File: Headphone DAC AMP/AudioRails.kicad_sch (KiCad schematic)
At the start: 39 parts, among them U11 ADP5071AREZ-R7, U12 TPS74501PDRVR, U14 ADP7185ACPZN-R7

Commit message: Swapped to 0603 caps in order to compact design
Planning on a 100x70mm board shape
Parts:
- C33, C34, C35, C36, C37, C38, C40, C41, C42, C43, C50, C51, C52, C53, C54, C55: footprint Capacitor_SMD:C_0805_2012Metric_Pad1.18x1.45mm_HandSolder -> Capacitor_SMD:C_0603_1608Metric_Pad1.08x0.95mm_HandSolder
- D1, D2: footprint Diode_SMD:D_0805_2012Metric_Pad1.15x1.40mm_HandSolder -> Capacitor_SMD:C_0603_1608Metric_Pad1.08x0.95mm_HandSolder
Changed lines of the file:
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@@
 			)
 		)
-		(property "Footprint" "Capacitor_SMD:C_0805_2012Metric_Pad1.18x1.45mm_HandSolder"
+		(property "Footprint" "Capacitor_SMD:C_0603_1608Metric_Pad1.08x0.95mm_HandSolder"
 			(at 50.4952 68.58 0)
 			(effects
@@
 			)
 		)
-		(property "Footprint" "Capacitor_SMD:C_0805_2012Metric_Pad1.18x1.45mm_HandSolder"
+		(property "Footprint" "Capacitor_SMD:C_0603_1608Metric_Pad1.08x0.95mm_HandSolder"
 			(at 28.9052 130.81 0)
 			(effects
@@
 			)
 		)
-		(property "Footprint" "Capacitor_SMD:C_0805_2012Metric_Pad1.18x1.45mm_HandSolder"
+		(property "Footprint" "Capacitor_SMD:C_0603_1608Metric_Pad1.08x0.95mm_HandSolder"
 			(at 185.1152 134.62 0)
 			(effects
@@
 			)
 		)
-		(property "Footprint" "Capacitor_SMD:C_0805_2012Metric_Pad1.18x1.45mm_HandSolder"
+		(property "Footprint" "Capacitor_SMD:C_0603_1608Metric_Pad1.08x0.95mm_HandSolder"
 			(at 55.5752 33.02 0)
 			(effects
@@
 			)
 		)
-		(property "Footprint" "Capacitor_SMD:C_0805_2012Metric_Pad1.18x1.45mm_HandSolder"
+		(property "Footprint" "Capacitor_SMD:C_0603_1608Metric_Pad1.08x0.95mm_HandSolder"
 			(at 142.24 42.2148 0)
 			(effects
@@
 			)
 		)
-		(property "Footprint" "Capacitor_SMD:C_0805_2012Metric_Pad1.18x1.45mm_HandSolder"
+		(property "Footprint" "Capacitor_SMD:C_0603_1608Metric_Pad1.08x0.95mm_HandSolder"
 			(at 130.5052 73.66 0)
 			(effects
@@
 			)
 		)
-		(property "Footprint" "Capacitor_SMD:C_0805_2012Metric_Pad1.18x1.45mm_HandSolder"
+		(property "Footprint" "Capacitor_SMD:C_0603_1608Metric_Pad1.08x0.95mm_HandSolder"
 			(at 247.3452 132.08 0)
 			(effects
@@
 			)
 		)
-		(property "Footprint" "Capacitor_SMD:C_0805_2012Metric_Pad1.18x1.45mm_HandSolder"
+		(property "Footprint" "Capacitor_SMD:C_0603_1608Metric_Pad1.08x0.95mm_HandSolder"
 			(at 174.9552 134.62 0)
 			(effects
@@
 			)
 		)
-		(property "Footprint" "Capacitor_SMD:C_0805_2012Metric_Pad1.18x1.45mm_HandSolder"
+		(property "Footprint" "Capacitor_SMD:C_0603_1608Metric_Pad1.08x0.95mm_HandSolder"
 			(at 159.7152 45.72 0)
 			(effects
@@
 			)
 		)
-		(property "Footprint" "Capacitor_SMD:C_0805_2012Metric_Pad1.18x1.45mm_HandSolder"
+		(property "Footprint" "Capacitor_SMD:C_0603_1608Metric_Pad1.08x0.95mm_HandSolder"
 			(at 40.3352 130.81 0)
 			(effects
@@
 			)
 		)
-		(property "Footprint" "Capacitor_SMD:C_0805_2012Metric_Pad1.18x1.45mm_HandSolder"
+		(property "Footprint" "Capacitor_SMD:C_0603_1608Metric_Pad1.08x0.95mm_HandSolder"
 			(at 63.1952 140.97 0)
 			(effects
@@
 			)
 		)
-		(property "Footprint" "Capacitor_SMD:C_0805_2012Metric_Pad1.18x1.45mm_HandSolder"
+		(property "Footprint" "Capacitor_SMD:C_0603_1608Metric_Pad1.08x0.95mm_HandSolder"
 			(at 125.4252 33.02 0)
 			(effects
@@
 			)
 		)
-		(property "Footprint" "Capacitor_SMD:C_0805_2012Metric_Pad1.18x1.45mm_HandSolder"
+		(property "Footprint" "Capacitor_SMD:C_0603_1608Metric_Pad1.08x0.95mm_HandSolder"
 			(at 130.5052 132.08 0)
 			(effects
@@
 			)
 		)
-		(property "Footprint" "Capacitor_SMD:C_0805_2012Metric_Pad1.18x1.45mm_HandSolder"
+		(property "Footprint" "Capacitor_SMD:C_0603_1608Metric_Pad1.08x0.95mm_HandSolder"
 			(at 120.3452 132.08 0)
 			(effects
@@
 			)
 		)
-		(property "Footprint" "Diode_SMD:D_0805_2012Metric_Pad1.15x1.40mm_HandSolder"
+		(property "Footprint" "Capacitor_SMD:C_0603_1608Metric_Pad1.08x0.95mm_HandSolder"
 			(at 43.18 33.02 0)
 			(effects
@@
 			)
 		)
-		(property "Footprint" "Capacitor_SMD:C_0805_2012Metric_Pad1.18x1.45mm_HandSolder"
+		(property "Footprint" "Capacitor_SMD:C_0603_1608Metric_Pad1.08x0.95mm_HandSolder"
 			(at 257.5052 132.08 0)
 			(effects
@@
 			)
 		)
-		(property "Footprint" "Capacitor_SMD:C_0805_2012Metric_Pad1.18x1.45mm_HandSolder"
+		(property "Footprint" "Capacitor_SMD:C_0603_1608Metric_Pad1.08x0.95mm_HandSolder"
 			(at 143.2052 132.08 0)
 			(effects
@@
 			)
 		)
-		(property "Footprint" "Diode_SMD:D_0805_2012Metric_Pad1.15x1.40mm_HandSolder"
+		(property "Footprint" "Capacitor_SMD:C_0603_1608Metric_Pad1.08x0.95mm_HandSolder"
 			(at 138.43 33.02 0)
 			(effects

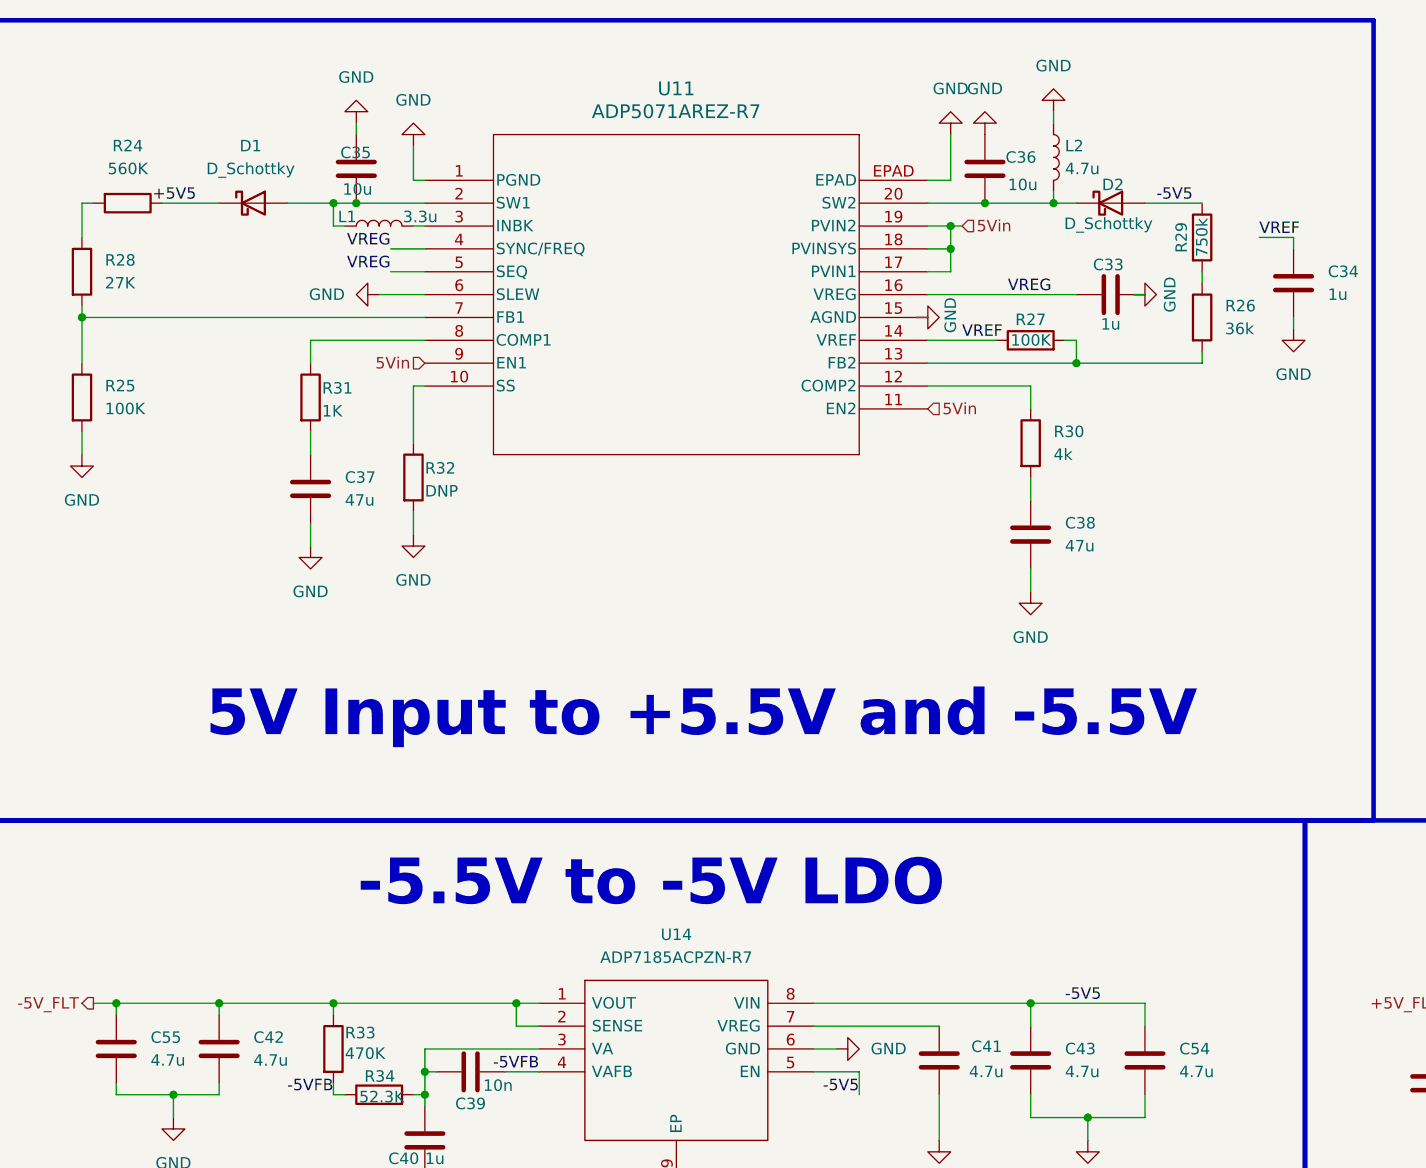
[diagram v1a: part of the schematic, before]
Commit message: Defined board shape and redid ADP5071 layout
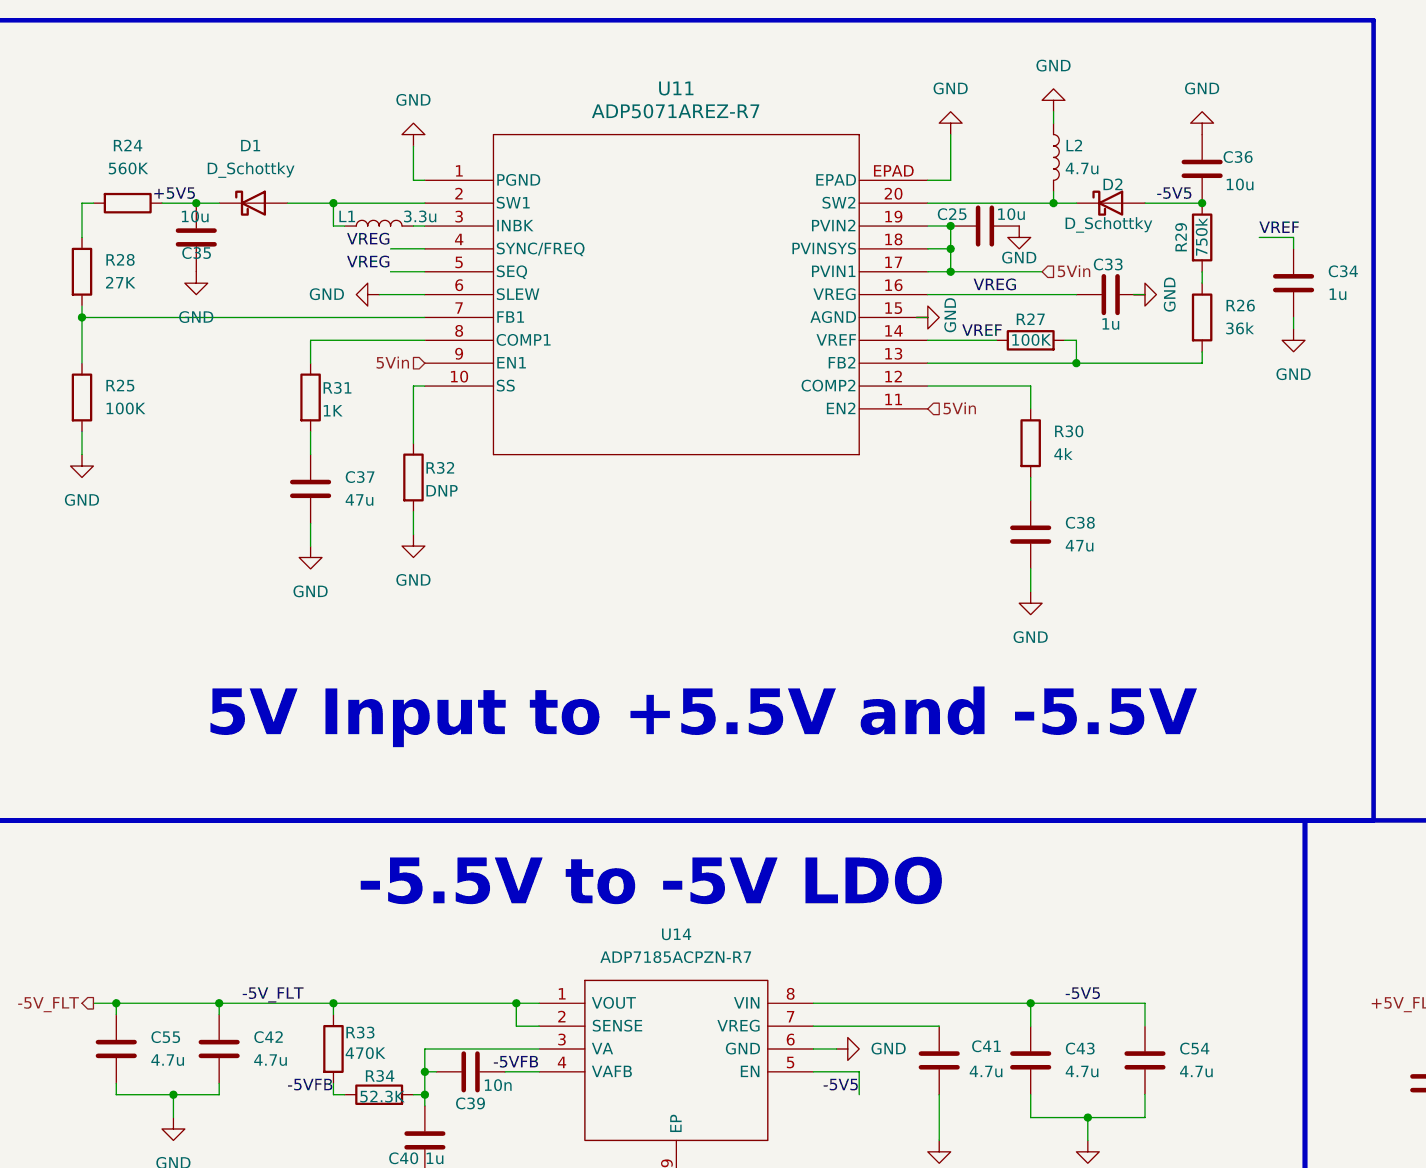
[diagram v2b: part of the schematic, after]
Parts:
- added C25: 10u, Capacitor_SMD:C_0603_1608Metric_Pad1.08x0.95mm_HandSolder, symbol Device:C
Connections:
- net +5V5: now also C35.2
- net -5V5: now also C36.2
- net 5Vin: now also C25.2
- net GND: now also C25.1
- net at D1.2 (A), L1.1, U11.2 (SW1): no longer C35.2
- net at D2.1 (K), L2.2, U11.20 (SW2): no longer C36.2
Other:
- moved on the sheet: C35, C36
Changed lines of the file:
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@@
 	)
 	(junction
+		(at 148.59 33.02)
+		(diameter 0)
+		(color 0 0 0 0)
+	)
+	(junction
 		(at 120.65 38.1)
 		(diameter 0)
@@
 	)
 	(junction
+		(at 120.65 40.64)
+		(diameter 0)
+		(color 0 0 0 0)
+	)
+	(junction
 		(at 62.23 132.08)
 		(diameter 0)
@@
 	)
 	(junction
-		(at 54.61 33.02)
-		(diameter 0)
-		(color 0 0 0 0)
-	)
-	(junction
 		(at 135.89 134.62)
 		(diameter 0)
@@
 	)
 	(junction
-		(at 124.46 33.02)
+		(at 36.83 33.02)
 		(diameter 0)
 		(color 0 0 0 0)
@@
 	(wire
 		(pts
-			(xy 54.61 24.13) (xy 54.61 25.4)
-		)
-		(stroke
-			(width 0)
-			(type default)
-		)
-	)
-	(wire
-		(pts
 			(xy 179.07 135.89) (xy 184.15 135.89)
 		)
@@
 	(wire
 		(pts
-			(xy 33.02 33.02) (xy 39.37 33.02)
+			(xy 33.02 33.02) (xy 36.83 33.02)
 		)
 		(stroke
@@
 	(wire
 		(pts
-			(xy 120.65 35.56) (xy 121.92 35.56)
+			(xy 120.65 40.64) (xy 130.81 40.64)
 		)
 		(stroke
@@
 	(wire
 		(pts
+			(xy 120.65 38.1) (xy 120.65 35.56)
+		)
+		(stroke
+			(width 0)
+			(type default)
+		)
+	)
+	(wire
+		(pts
 			(xy 270.51 135.89) (xy 270.51 137.16)
 		)
@@
 	(wire
 		(pts
-			(xy 124.46 33.02) (xy 132.08 33.02)
+			(xy 118.11 33.02) (xy 132.08 33.02)
 		)
 		(stroke
@@
 	(wire
 		(pts
-			(xy 52.07 33.02) (xy 54.61 33.02)
+			(xy 52.07 33.02) (xy 62.23 33.02)
 		)
 		(stroke
@@
 	(wire
 		(pts
-			(xy 118.11 33.02) (xy 124.46 33.02)
-		)
-		(stroke
-			(width 0)
-			(type default)
-		)
-	)
-	(wire
-		(pts
 			(xy 58.42 38.1) (xy 62.23 38.1)
 		)
@@
 	(wire
 		(pts
-			(xy 120.65 35.56) (xy 120.65 38.1)
-		)
-		(stroke
-			(width 0)
-			(type default)
-		)
-	)
-	(wire
-		(pts
-			(xy 54.61 33.02) (xy 62.23 33.02)
+			(xy 36.83 33.02) (xy 39.37 33.02)
 		)
 		(stroke
@@
 	)
 	(label "VREG"
-		(at 127 43.18 0)
+		(at 123.19 43.18 0)
 		(effects
 			(font
@@
 		)
 	)
+	(label "-5V_FLT"
+		(at 41.91 121.92 0)
+		(effects
+			(font
+				(size 1.27 1.27)
+			)
+			(justify left bottom)
+		)
+	)
 	(label "5VFB"
 		(at 198.12 124.46 0)
@@
 	(hierarchical_label "5Vin"
 		(shape input)
-		(at 121.92 35.56 0)
+		(at 130.81 40.64 0)
 		(effects
 			(font
@@
 	)
 	(symbol
+		(lib_id "Device:C")
+		(at 124.46 35.56 270)
+		(unit 1)
+		(exclude_from_sim no)
+		(in_bom yes)
+		(on_board yes)
+		(dnp no)
+		(property "Reference" "C25"
+			(at 119.126 34.29 90)
+			(effects
+				(font
+					(size 1.27 1.27)
+				)
+				(justify left)
+			)
+		)
+		(property "Value" "10u"
+			(at 125.73 34.29 90)
+			(effects
+				(font
+					(size 1.27 1.27)
+				)
+				(justify left)
+			)
+		)
+		(property "Footprint" "Capacitor_SMD:C_0603_1608Metric_Pad1.08x0.95mm_HandSolder"
+			(at 120.65 36.5252 0)
+			(effects
+				(font
+					(size 1.27 1.27)
+				)
+				(hide yes)
+			)
+		)
+		(property "Datasheet" "~"
+			(at 124.46 35.56 0)
+			(effects
+				(font
+					(size 1.27 1.27)
+				)
+				(hide yes)
+			)
+		)
+		(property "Description" "Unpolarized capacitor"
+			(at 124.46 35.56 0)
+			(effects
+				(font
+					(size 1.27 1.27)
+				)
+				(hide yes)
+			)
+		)
+		(pin "2"
+		)
+		(pin "1"
+		)
+		(instances
+			(project "Headphone DAC AMP"
+				(path "/d034eddd-efbc-47be-a25c-37cbfbab4cd8/22bf93f4-b6c7-483e-b255-2ccf5bc3f52b"
+					(reference "C25")
+					(unit 1)
+				)
+			)
+		)
+	)
+	(symbol
 		(lib_id "power:GND")
 		(at 270.51 137.16 0)
@@
 	(symbol
 		(lib_id "Device:C")
-		(at 54.61 29.21 0)
+		(at 36.83 36.83 180)
 		(unit 1)
 		(exclude_from_sim no)
@@
 		(dnp no)
 		(property "Reference" "C35"
-			(at 52.832 27.432 0)
+			(at 38.608 38.608 0)
 			(effects
 				(font
@@
 		)
 		(property "Value" "10u"
-			(at 53.086 31.496 0)
+			(at 38.354 34.544 0)
 			(effects
 				(font
@@
 		)
 		(property "Footprint" "Capacitor_SMD:C_0603_1608Metric_Pad1.08x0.95mm_HandSolder"
-			(at 55.5752 33.02 0)
+			(at 35.8648 33.02 0)
 			(effects
 				(font
@@
 		)
 		(property "Datasheet" "~"
-			(at 54.61 29.21 0)
+			(at 36.83 36.83 0)
 			(effects
 				(font
@@
 		)
 		(property "Description" "Unpolarized capacitor"
-			(at 54.61 29.21 0)
+			(at 36.83 36.83 0)
 			(effects
 				(font
@@
 	(symbol
 		(lib_id "power:GND")
-		(at 124.46 25.4 180)
+		(at 148.59 25.4 180)
 		(unit 1)
 		(exclude_from_sim no)
@@
 		(fields_autoplaced yes)
 		(property "Reference" "#PWR043"
-			(at 124.46 19.05 0)
+			(at 148.59 19.05 0)
 			(effects
 				(font
@@
 		)
 		(property "Value" "GND"
-			(at 124.46 20.32 0)
+			(at 148.59 20.32 0)
 			(effects
 				(font
@@
 		)
 		(property "Footprint" ""
-			(at 124.46 25.4 0)
+			(at 148.59 25.4 0)
 			(effects
 				(font
@@
 		)
 		(property "Datasheet" ""
-			(at 124.46 25.4 0)
+			(at 148.59 25.4 0)
 			(effects
 				(font
@@
 		)
 		(property "Description" "Power symbol creates a global label with name \"GND\" , ground"
-			(at 124.46 25.4 0)
+			(at 148.59 25.4 0)
 			(effects
 				(font
@@
 	(symbol
 		(lib_id "Device:C")
-		(at 124.46 29.21 0)
+		(at 148.59 29.21 0)
 		(unit 1)
 		(exclude_from_sim no)
@@
 		(dnp no)
 		(property "Reference" "C36"
-			(at 126.746 27.94 0)
+			(at 150.876 27.94 0)
 			(effects
 				(font
@@
 		)
 		(property "Value" "10u"
-			(at 127 30.988 0)
+			(at 151.13 30.988 0)
 			(effects
 				(font
@@
 		)
 		(property "Footprint" "Capacitor_SMD:C_0603_1608Metric_Pad1.08x0.95mm_HandSolder"
-			(at 125.4252 33.02 0)
+			(at 149.5552 33.02 0)
 			(effects
 				(font
@@
 		)
 		(property "Datasheet" "~"
-			(at 124.46 29.21 0)
+			(at 148.59 29.21 0)
 			(effects
 				(font
@@
 		)
 		(property "Description" "Unpolarized capacitor"
-			(at 124.46 29.21 0)
+			(at 148.59 29.21 0)
 			(effects
 				(font
@@
 	(symbol
 		(lib_id "power:GND")
-		(at 54.61 24.13 180)
+		(at 36.83 40.64 0)
 		(unit 1)
 		(exclude_from_sim no)
@@
 		(fields_autoplaced yes)
 		(property "Reference" "#PWR042"
-			(at 54.61 17.78 0)
+			(at 36.83 46.99 0)
 			(effects
 				(font
@@
 		)
 		(property "Value" "GND"
-			(at 54.61 19.05 0)
+			(at 36.83 45.72 0)
 			(effects
 				(font
@@
 		)
 		(property "Footprint" ""
-			(at 54.61 24.13 0)
+			(at 36.83 40.64 0)
 			(effects
 				(font
@@
 		)
 		(property "Datasheet" ""
-			(at 54.61 24.13 0)
+			(at 36.83 40.64 0)
 			(effects
 				(font
@@
 		)
 		(property "Description" "Power symbol creates a global label with name \"GND\" , ground"
-			(at 54.61 24.13 0)
+			(at 36.83 40.64 0)
 			(effects
 				(font
@@
 					(unit 1)
 				)
+			)
+		)
+	)
+	(symbol
+		(lib_id "power:GND")
+		(at 128.27 35.56 0)
+		(unit 1)
+		(exclude_from_sim no)
+		(in_bom yes)
+		(on_board yes)
+		(dnp no)
+		(property "Reference" "#PWR031"
+			(at 128.27 41.91 0)
+			(effects
+				(font
+					(size 1.27 1.27)
+				)
+				(hide yes)
+			)
+		)
+		(property "Value" "GND"
+			(at 128.27 39.116 0)
+			(effects
+				(font
+					(size 1.27 1.27)
+				)
+			)
+		)
+		(property "Footprint" ""
+			(at 128.27 35.56 0)
+			(effects
+				(font
+					(size 1.27 1.27)
+				)
+				(hide yes)
+			)
+		)
+		(property "Datasheet" ""
+			(at 128.27 35.56 0)
+			(effects
+				(font
+					(size 1.27 1.27)
+				)
+				(hide yes)
+			)
+		)
+		(property "Description" "Power symbol creates a global label with name \"GND\" , ground"
+			(at 128.27 35.56 0)
+			(effects
+				(font
+					(size 1.27 1.27)
+				)
+				(hide yes)
+			)
+		)
+		(pin "1"
+		)
+		(instances
+			(project "Headphone DAC AMP"
+				(path "/d034eddd-efbc-47be-a25c-37cbfbab4cd8/22bf93f4-b6c7-483e-b255-2ccf5bc3f52b"
+					(reference "#PWR031")
+					(unit 1)
+				)
